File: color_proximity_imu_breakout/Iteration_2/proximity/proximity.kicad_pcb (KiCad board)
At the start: 2 copper layers, 12.6 x 16.5 mm, 10 parts, among them IC1 VL53L4CDV0DH_1, J4 Conn_01x05

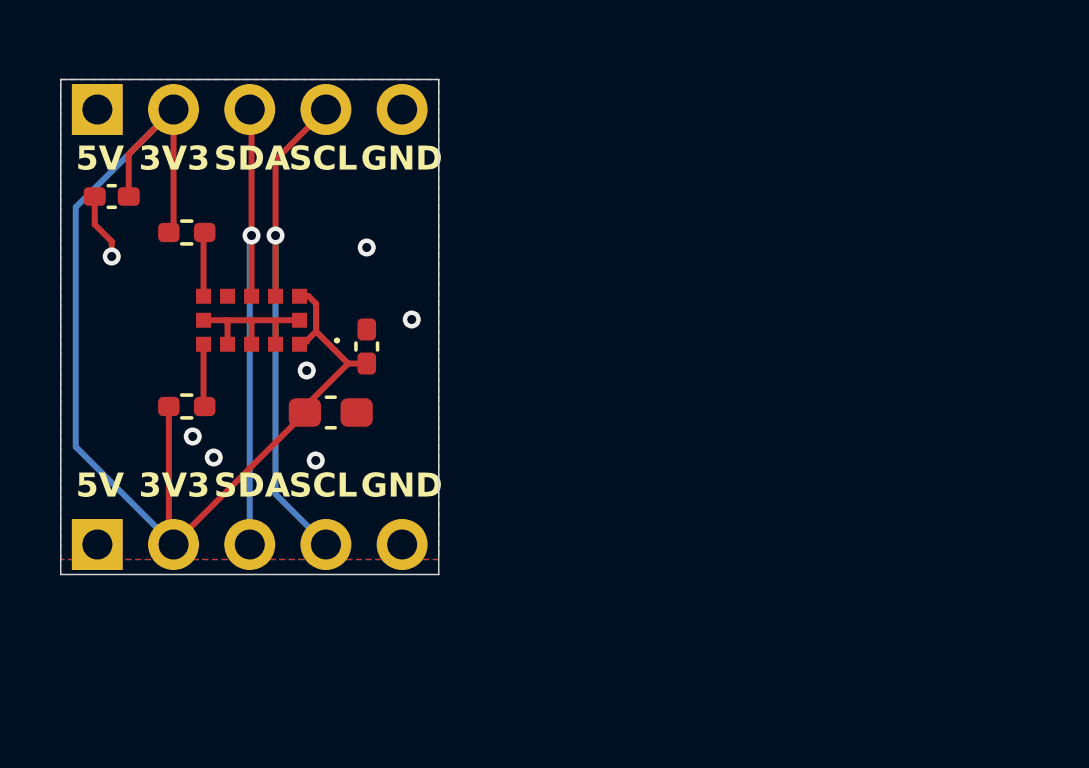
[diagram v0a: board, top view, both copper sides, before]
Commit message: proximity board iteration 2 updated
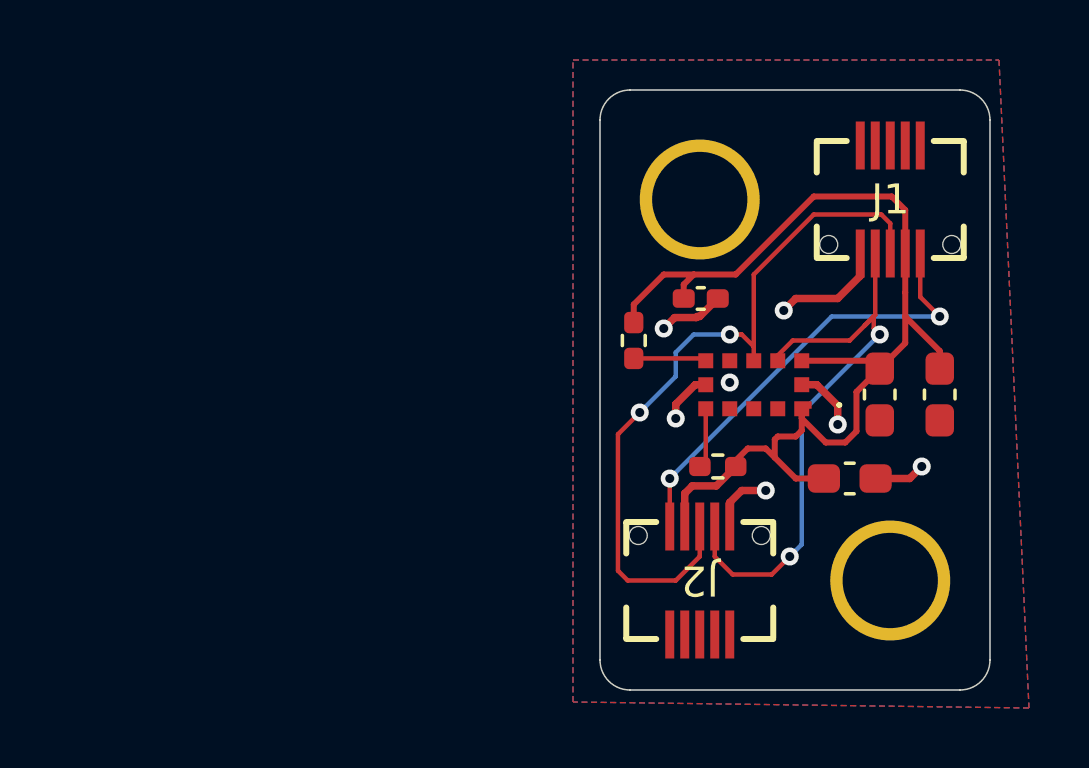
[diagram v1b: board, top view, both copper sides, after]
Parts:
- removed the G*** at (124.5, 113.2)
- removed the G*** at (122.9, 108.4)
- removed J4 (x2): Conn_01x05, Connector_PinHeader_2.54mm:PinHeader_1x05_P2.54mm_Vertical
- added ?: , , F.Cu at (147.9, 120.8)
- added ?: , , F.Cu at (141.6, 108.1)
- added C2: 10u, Capacitor_SMD:C_0603_1608Metric_Pad1.08x0.95mm_HandSolder, F.Cu at (149.6, 114.6)
- added G***: LOGO, LOGO, B.Cu at (109.2, 113.6)
- added G***: LOGO, LOGO, B.Cu at (112.4, 124.0)
- added J1: Conn_01x10, pcb_footprints:GT-B0502MSV27-10S1101, F.Cu at (147.9, 108.1)
- added J2: Conn_01x10, pcb_footprints:GT-B0502MSV27-10S1101, F.Cu at (141.6, 120.8)
- C1: footprint Capacitor_SMD:C_0402_1005Metric_Pad0.74x0.62mm_HandSolder -> Capacitor_SMD:C_0603_1608Metric_Pad1.08x0.95mm_HandSolder
- moved C1 26.4 mm to (147.6, 114.6), turned to 90 degrees
- moved R21 17.8 mm to (142.2, 117.0), turned to 180 degrees
- moved C12 17.4 mm to (146.6, 117.4)
- moved IC1 16.9 mm to (143.4, 114.3)
- moved R20 15.3 mm to (139.4, 112.8), turned to 90 degrees
- moved C11 11.2 mm to (141.6, 111.4), turned to 0 degrees
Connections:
- C1 pad 1: +3.3V -> GND
- C1 pad 2: GND -> +3.3V
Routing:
- net +5V: track 0.02 -> 15.2 mm, vias 0 -> 2
- net /sda: track 16.7 -> 24.7 mm, vias 1 -> 2
- net GND: track 7.90 -> 13.7 mm
- net +3.3V: track 42.7 -> 37.2 mm
- net /scl: track 17.9 -> 19.8 mm, vias 1 -> 2
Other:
- board size 12.6 x 16.5 mm -> 13 x 20 mm
- board text removed: "3V3"
- board text removed: "5V"
- board text removed: "GND"
- board text removed: "SCL"
- board text removed: "SDA"

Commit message: breakout board iteration 2 updates
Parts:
- moved C12 1.60 mm to (145.0, 117.4)
- moved C11 0.40 mm to (141.6, 111.8)
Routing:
- net GND: track 13.7 -> 14.6 mm

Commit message: finished base board PCB + created production files for base board and modules
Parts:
- moved G*** 38.2 mm to (146.8, 107.3)
- moved G*** 33.3 mm to (141.6, 121.5)
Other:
- board text added: "Designed By Gengwen Li Trung Le"
- board text removed: "Designed By Gengwen Li"
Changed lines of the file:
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@@
 	(footprint "LOGO"
 		(layer "B.Cu")
-		(at 109.2 113.6 180)
+		(at 141.6 121.5 180)
 		(property "Reference" "G***"
 			(at 0 0 0)
@@
 	(footprint "LOGO"
 		(layer "B.Cu")
-		(at 112.4 124 180)
+		(at 146.798384 107.296251 180)
 		(property "Reference" "G***"
 			(at 0 0 0)
@@
 		(layer "Edge.Cuts")
 	)
-	(gr_text "Designed By\nGengwen Li"
-		(at 127.4 127.4 0)
+	(gr_text "Designed By\nGengwen Li\nTrung Le"
+		(at 148.1 116.6 0)
 		(layer "B.SilkS")
 		(effects

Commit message: updated production files
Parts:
- removed the G*** at (141.6, 121.5)
- added G***: LOGO, GDLX-SMT-N-66:vexu_ghost, F.Cu at (146.9, 106.8)
- J1, J2: moved to B.Cu
- moved G*** 6.64 mm to (144.7, 113.6), turned to -145 degrees
- turned C1 to -90 degrees
- turned C2 to -90 degrees
- turned J1 to 180 degrees
- turned J2 to 0 degrees
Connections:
- C1 pad 1: GND -> +3.3V
- C1 pad 2: +3.3V -> GND
- C2 pad 1: GND -> +3.3V
- C2 pad 2: +3.3V -> GND
- J1 pad 10: +5V -> GND
- J1 pad 6: GND -> unconnected-(J1-Pin_6-Pad6)
- J1 pad 7: /scl -> +3.3V
- J1 pad 9: +3.3V -> /scl
- J2 pad 10: +5V -> GND
- J2 pad 6: GND -> unconnected-(J2-Pin_6-Pad6)
- J2 pad 7: /scl -> +3.3V
- J2 pad 9: +3.3V -> /scl
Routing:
- net +5V: track 15.2 -> 0.00 mm, vias 2 -> 0
- net GND: track 14.6 -> 21.7 mm, vias 7 -> 6
- net /scl: track 19.8 -> 15.0 mm, vias 2 -> 1
- net /sda: track 24.7 -> 20.6 mm, vias 2 -> 1
- net +3.3V: track 36.8 -> 40.4 mm, vias 0 -> 2
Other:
- board text added: "Designed By: Gengwen Li Trung Le"
- board text removed: "Designed By Gengwen Li Trung Le"
